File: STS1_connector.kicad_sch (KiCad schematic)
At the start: 2 parts

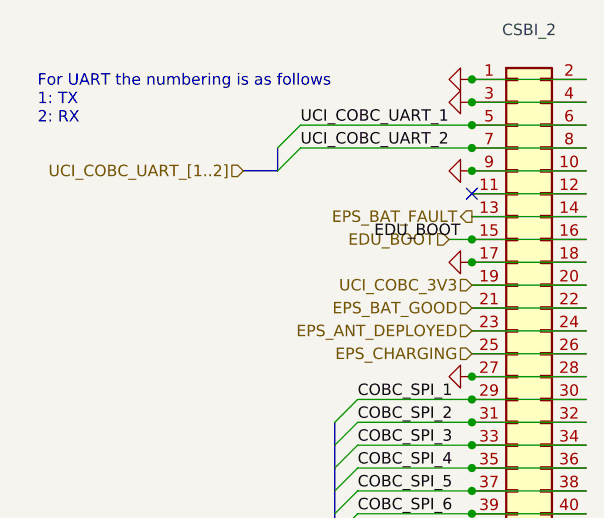
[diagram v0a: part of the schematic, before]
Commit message: more work done
All parts besides RF added
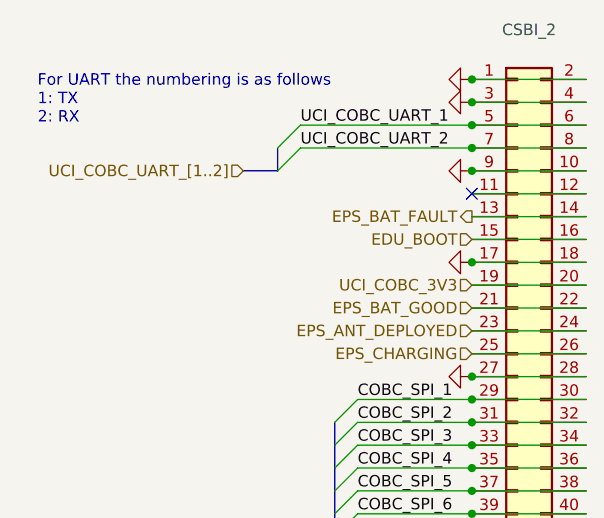
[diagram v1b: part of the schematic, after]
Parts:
- CSBI_1, CSBI_2: footprint (none) -> Connector_PinSocket_2.00mm:PinSocket_2x25_P2.00mm_Vertical
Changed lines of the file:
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@@
   (junction (at 87.63 72.39) (diameter 0) (color 0 0 0 0)
-  )
-  (junction (at 165.1 60.96) (diameter 0) (color 0 0 0 0)
   )
   (no_connect (at 87.63 80.01))
@@
     (stroke (width 0) (type default) (color 0 0 0 0))
   )
-  (wire (pts (xy 162.56 60.96) (xy 165.1 60.96))
-    (stroke (width 0) (type default) (color 0 0 0 0))
-  )
   (bus (pts (xy 67.31 78.74) (xy 62.23 78.74))
     (stroke (width 0) (type default) (color 0 0 0 0))
@@
     (effects (font (size 1.27 1.27)) (justify left bottom))
   )
-  (label "EDU_BOOT" (at 163.83 60.96 180)
-    (effects (font (size 1.27 1.27)) (justify right bottom))
-  )
   (label "COBC_SPI_2" (at 152.4 81.28 0)
     (effects (font (size 1.27 1.27)) (justify left bottom))
@@
     (effects (font (size 1.27 1.27)) (justify right))
   )
+  (hierarchical_label "EDU_BOOT" (shape input) (at 165.1 60.96 180)
+    (effects (font (size 1.27 1.27)) (justify right))
+  )
   (hierarchical_label "UCI_COBC_3V3" (shape input) (at 165.1 66.04 180)
     (effects (font (size 1.27 1.27)) (justify right))
@@
   )
   (hierarchical_label "EDU_Heartbeat" (shape input) (at 87.63 87.63 180)
-    (effects (font (size 1.27 1.27)) (justify right))
-  )
-  (hierarchical_label "EDU_BOOT" (shape input) (at 162.56 60.96 180)
     (effects (font (size 1.27 1.27)) (justify right))
   )
@@
     (property "Reference" "CSBI_1" (id 0) (at 93.98 38.9382 0))
     (property "Value" "~" (id 1) (at 93.98 41.2496 0))
-    (property "Footprint" "" (id 2) (at 92.71 74.93 0)
+    (property "Footprint" "Connector_PinSocket_2.00mm:PinSocket_2x25_P2.00mm_Vertical" (id 2) (at 92.71 74.93 0)
       (effects (font (size 1.27 1.27)) hide)
     )
@@
     (property "Reference" "CSBI_2" (id 0) (at 171.45 37.6682 0))
     (property "Value" "~" (id 1) (at 171.45 39.9796 0))
-    (property "Footprint" "" (id 2) (at 170.18 73.66 0)
+    (property "Footprint" "Connector_PinSocket_2.00mm:PinSocket_2x25_P2.00mm_Vertical" (id 2) (at 170.18 73.66 0)
       (effects (font (size 1.27 1.27)) hide)
     )

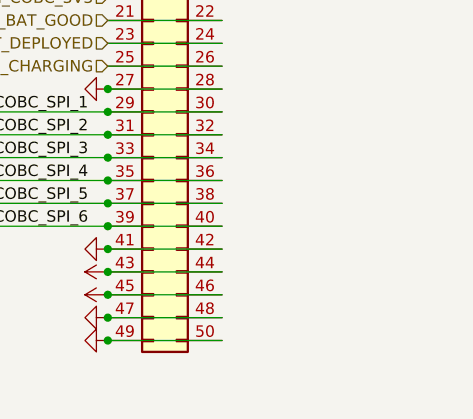
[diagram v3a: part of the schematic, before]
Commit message: Remove old submodules
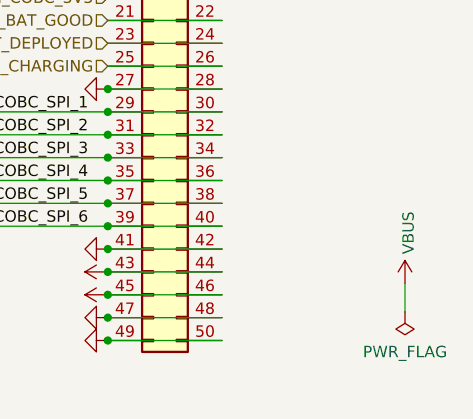
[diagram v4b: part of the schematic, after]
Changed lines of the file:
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@@
+    (stroke (width 0) (type default) (color 0 0 0 0))
+  )
+  (wire (pts (xy 198.12 97.79) (xy 198.12 100.965))
     (stroke (width 0) (type default) (color 0 0 0 0))
   )
@@
       (effects (font (size 1.27 1.27)) hide)
     )
+    (pin "1")
+  )
+  (symbol (lib_id "power:PWR_FLAG") (at 198.12 100.965 180) (unit 1)
+    (in_bom yes) (on_board yes) (fields_autoplaced)
+    (property "Reference" "#FLG0102" (id 0) (at 198.12 102.87 0)
+      (effects (font (size 1.27 1.27)) hide)
+    )
+    (property "Value" "PWR_FLAG" (id 1) (at 198.12 105.41 0))
+    (property "Footprint" "" (id 2) (at 198.12 100.965 0)
+      (effects (font (size 1.27 1.27)) hide)
+    )
+    (property "Datasheet" "~" (id 3) (at 198.12 100.965 0)
+      (effects (font (size 1.27 1.27)) hide)
+    )
+    (pin "1")
+  )
+  (symbol (lib_id "power:VBUS") (at 198.12 97.79 0) (unit 1)
+    (in_bom yes) (on_board yes)
+    (property "Reference" "#PWR0193" (id 0) (at 198.12 101.6 0)
+      (effects (font (size 1.27 1.27)) hide)
+    )
+    (property "Value" "VBUS" (id 1) (at 198.501 94.5642 90)
+      (effects (font (size 1.27 1.27)) (justify left))
+    )
+    (property "Footprint" "" (id 2) (at 198.12 97.79 0)
+      (effects (font (size 1.27 1.27)) hide)
+    )
+    (property "Datasheet" "" (id 3) (at 198.12 97.79 0)
+      (effects (font (size 1.27 1.27)) hide)
+    )

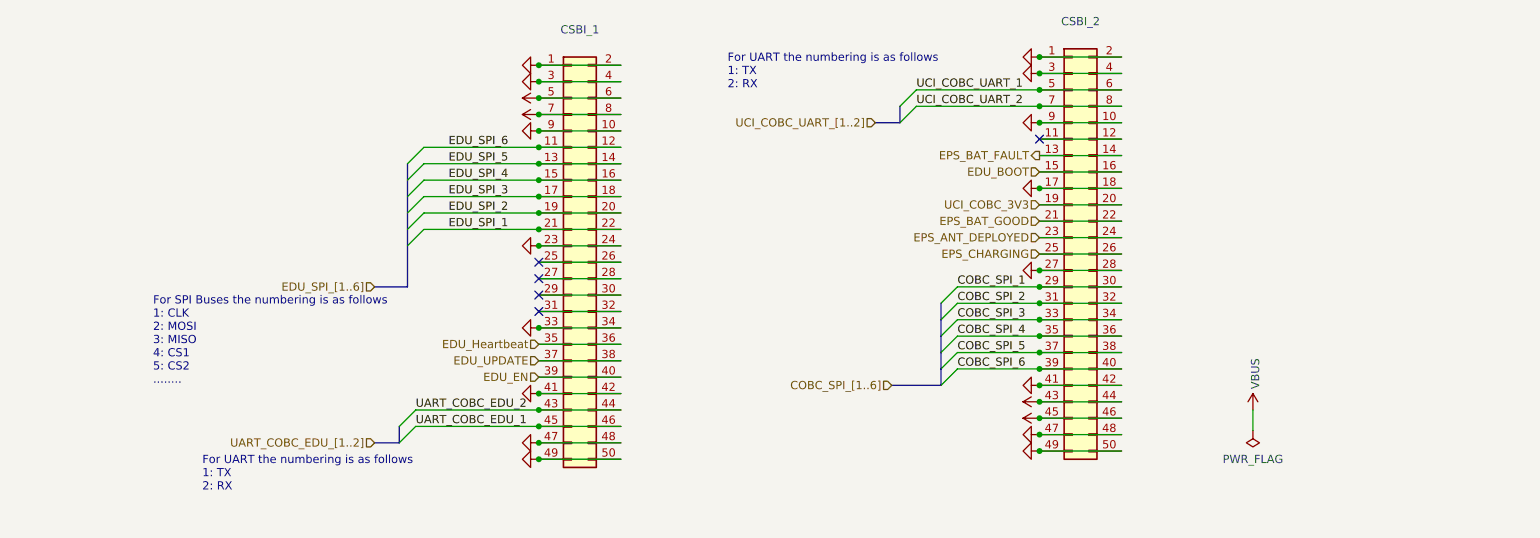
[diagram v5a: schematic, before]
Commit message: feat: clean up schematic
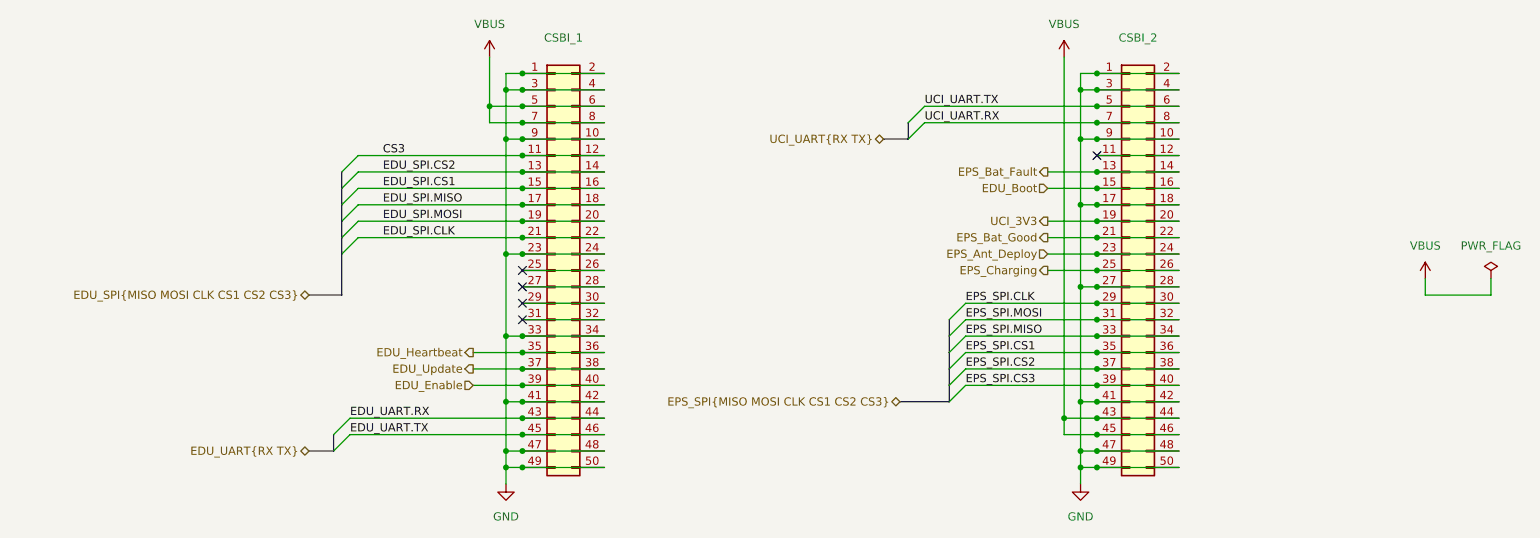
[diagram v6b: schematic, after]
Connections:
- net COBC_SPI_1 renamed EPS_SPI.CLK
- net COBC_SPI_2 renamed EPS_SPI.MOSI
- net COBC_SPI_3 renamed EPS_SPI.MISO
- net COBC_SPI_4 renamed EPS_SPI.CS1
- net COBC_SPI_5 renamed EPS_SPI.CS2
- net COBC_SPI_6 renamed EPS_SPI.CS3
- net EDU_BOOT renamed EDU_Boot
- net EDU_EN renamed EDU_Enable
- net EDU_SPI_1 renamed EDU_SPI.CLK
- net EDU_SPI_2 renamed EDU_SPI.MOSI
- net EDU_SPI_3 renamed EDU_SPI.MISO
- net EDU_SPI_4 renamed EDU_SPI.CS1
- net EDU_SPI_5 renamed EDU_SPI.CS2
- net EDU_SPI_6 renamed CS3
- net EDU_UPDATE renamed EDU_Update
- net EPS_ANT_DEPLOYED renamed EPS_Ant_Deploy
- net EPS_BAT_FAULT renamed EPS_Bat_Fault
- net EPS_BAT_GOOD renamed EPS_Bat_Good
- net EPS_CHARGING renamed EPS_Charging
- net UART_COBC_EDU_1 renamed EDU_UART.TX
- net UART_COBC_EDU_2 renamed EDU_UART.RX
- net UCI_COBC_3V3 renamed UCI_3V3
- net UCI_COBC_UART_1 renamed UCI_UART.TX
- net UCI_COBC_UART_2 renamed UCI_UART.RX
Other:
- note removed: "For SPI Buses the numbering is as follows 1: CLK 2: MOSI 3: MISO 4: CS1 5: CS2 ........"
- note removed: "For UART the numbering is as follows 1: TX 2: RX"
- moved on the sheet: CSBI_1, CSBI_2

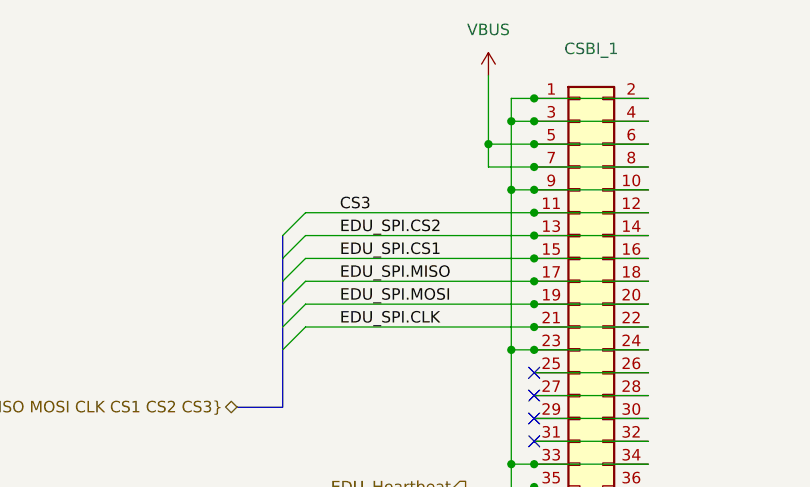
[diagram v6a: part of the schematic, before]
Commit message: feat: update RF hardware and clean up ERC errors
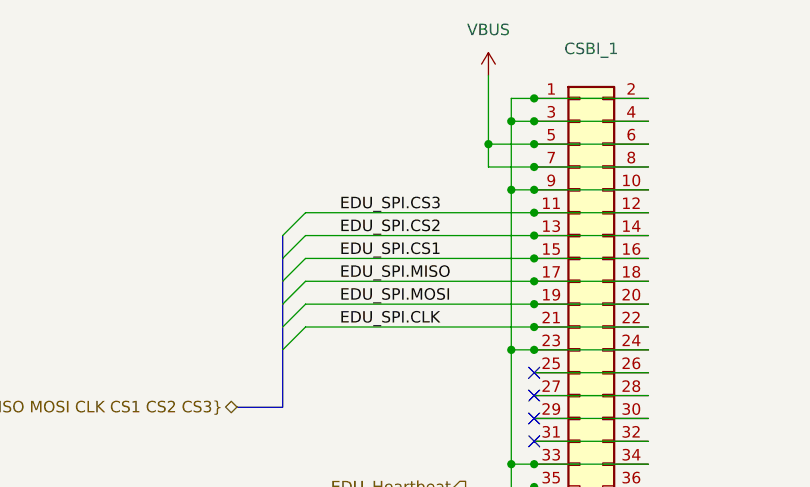
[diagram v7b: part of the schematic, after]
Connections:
- net CS3 renamed EDU_SPI.CS3
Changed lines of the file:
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@@
     (effects (font (size 1.27 1.27)) (justify left bottom))
   )
-  (label "CS3" (at 63.5 58.42 0)
+  (label "EDU_SPI.CS3" (at 63.5 58.42 0)
     (effects (font (size 1.27 1.27)) (justify left bottom))
   )
@@
     (pin "9")
   )
-  (symbol (lib_name "VBUS_1") (lib_id "power:VBUS") (at 80.01 43.18 0) (unit 1)
+  (symbol (lib_id "power:VBUS") (at 80.01 43.18 0) (unit 1)
     (in_bom yes) (on_board yes) (fields_autoplaced)
     (property "Reference" "#PWR0120" (id 0) (at 80.01 46.99 0)
@@
     (pin "1")
   )
-  (symbol (lib_name "VBUS_1") (lib_id "power:VBUS") (at 224.79 77.47 0) (unit 1)
+  (symbol (lib_id "power:VBUS") (at 224.79 77.47 0) (unit 1)
     (in_bom yes) (on_board yes) (fields_autoplaced)
     (property "Reference" "#PWR0122" (id 0) (at 224.79 81.28 0)
@@
     (pin "1")
   )
-  (symbol (lib_name "VBUS_1") (lib_id "power:VBUS") (at 168.91 43.18 0) (unit 1)
+  (symbol (lib_id "power:VBUS") (at 168.91 43.18 0) (unit 1)
     (in_bom yes) (on_board yes) (fields_autoplaced)
     (property "Reference" "#PWR0118" (id 0) (at 168.91 46.99 0)
